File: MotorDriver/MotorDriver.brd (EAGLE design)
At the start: 50 x 50 mm, 52 parts, among them CN1 53375-0610, Q1 BUK7Y7R8-80EX, Q2 BUK7Y7R8-80EX, Q3 BUK7Y7R8-80EX, Q4 BUK7Y7R8-80EX, Q5 BUK7Y7R8-80EX, Q6 BUK7Y7R8-80EX, U1 LPC1549JBD48, U2 DRV8320SRTVT, U3 MCP1700T-33, U4 ADR5041

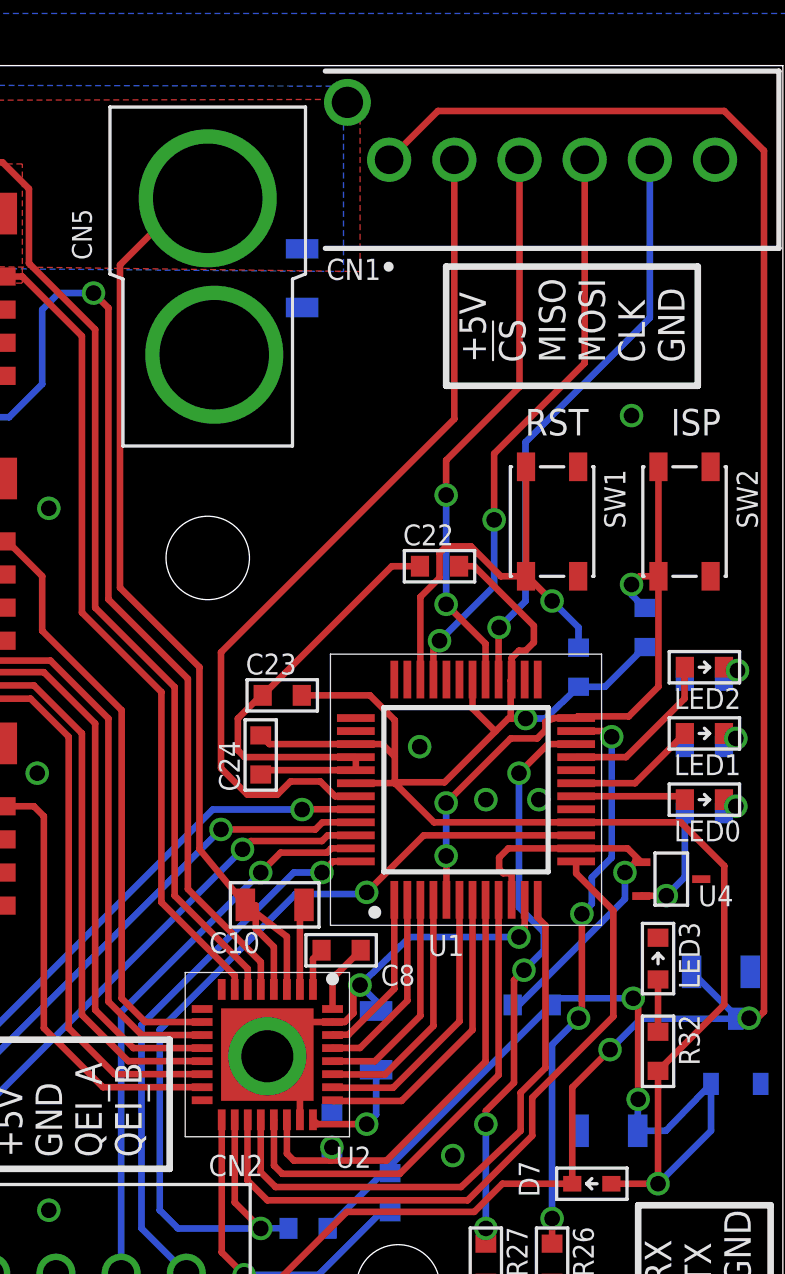
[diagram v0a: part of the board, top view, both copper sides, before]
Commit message: SCT1_OUT[5, 6]を使うために配線を入れ替えた
1:    PWM_CL->MOSI
2:    PWM_CH->RX
22: RX->PWM_CH
33  MOSI->PWM_CL
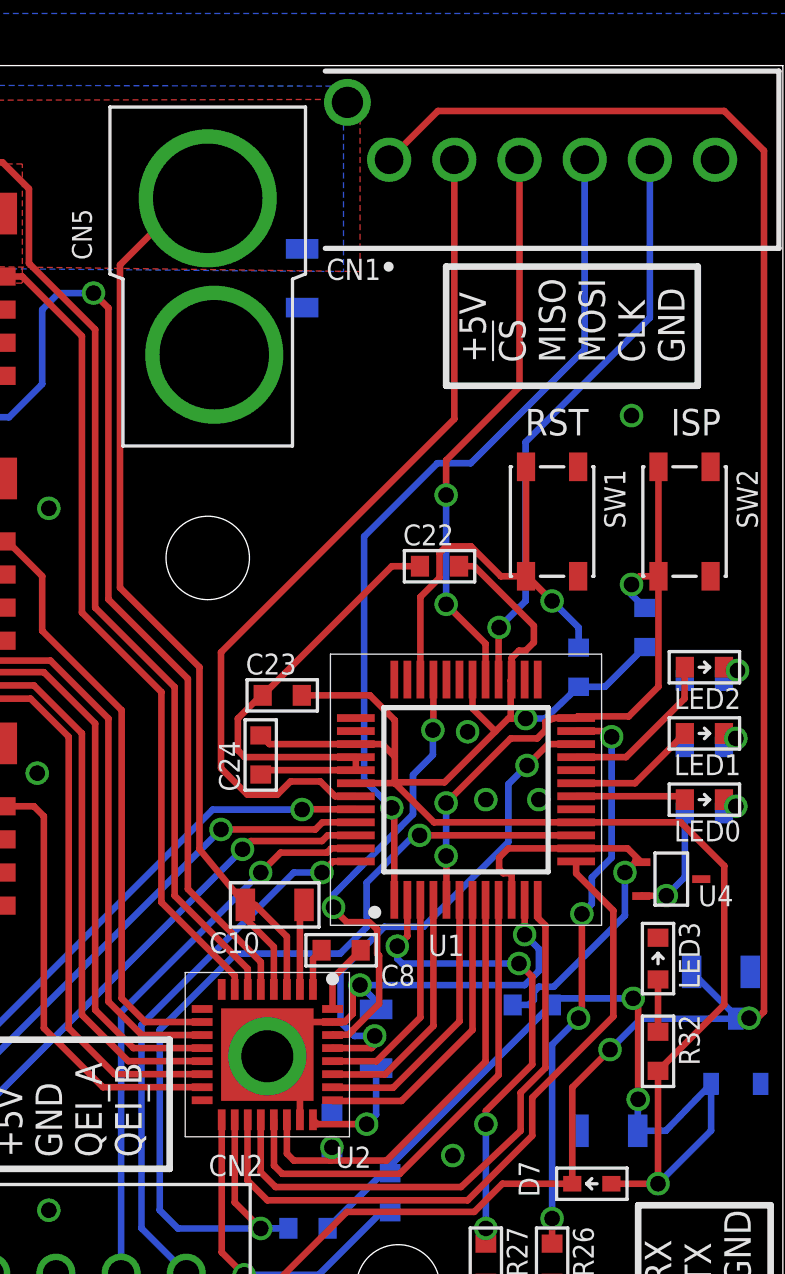
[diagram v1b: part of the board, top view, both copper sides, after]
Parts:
- moved C9 0.06 mm to (34.4, 12.7)
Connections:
- net MOSI: now also U1.1; no longer U1.33
- net PWM_CH: now also U1.22; no longer U1.2
- net PWM_CL: now also U1.33; no longer U1.1
- net RX: now also U1.2; no longer U1.22
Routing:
- net PWM_CH: track 7.49 -> 19.5 mm, vias 0 -> 2
- net PWM_CL: track 6.52 -> 17.5 mm, vias 0 -> 2
- net MOSI: track 22.3 -> 33.1 mm, vias 2 -> 1
- net RX: track 22.0 -> 18.8 mm
- net GND: track 42.2 -> 43.9 mm
- net SDO: track 35.8 -> 36.8 mm
- net VREF: track 15.6 -> 16.2 mm

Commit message: FETのゲートソース間に抵抗を追加
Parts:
- added R10, R11, R12, R7, R8, R9: 10k, Passive:1608
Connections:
- net GH_A: now also R11.2
- net GH_B: now also R9.2
- net GH_C: now also R7.2
- net GL_A: now also R12.2
- net GL_B: now also R10.2
- net GL_C: now also R8.2
- net GND: now also R10.1, R12.1, R8.1
- net SH_A: now also R11.1
- net SH_B: now also R9.1
- net SH_C: now also R7.1
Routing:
- net GND: track 43.9 -> 45.6 mm, vias 14 -> 15
- net GL_B: track 23.1 -> 24.8 mm, vias 0 -> 1
- net GL_C: track 17.0 -> 18.6 mm, vias 0 -> 1
- net GL_A: track 31.6 -> 33.2 mm, vias 0 -> 1
- net SH_C: track 26.3 -> 27.7 mm
- net GH_C: track 31.3 -> 32.7 mm, vias 0 -> 1
- net GH_B: track 33.2 -> 34.1 mm, vias 0 -> 1
- net GH_A: track 52.2 -> 53.2 mm
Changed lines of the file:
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@@
 <attribute name="VALUE" x="24.13" y="35.56" size="0.762" layer="27" font="vector" ratio="17" rot="R90"/>
 </element>
+<element name="R7" library="Passive" package="1608" value="10k" x="13.46875" y="25" rot="MR90"/>
+<element name="R8" library="Passive" package="1608" value="10k" x="18.4375" y="20.625" rot="MR90"/>
+<element name="R9" library="Passive" package="1608" value="10k" x="11.25" y="26.53125" rot="MR180"/>
+<element name="R10" library="Passive" package="1608" value="10k" x="18.4375" y="30.625" rot="MR90"/>
+<element name="R11" library="Passive" package="1608" value="10k" x="11.5625" y="36.5625" rot="MR270"/>
+<element name="R12" library="Passive" package="1608" value="10k" x="18.4375" y="40.9375" rot="MR90"/>
 </elements>
 <signals>
@@
 <via x="15.24" y="40.005" extent="1-16" drill="0.6" shape="octagon"/>
 <via x="15.24" y="41.275" extent="1-16" drill="0.6" shape="octagon"/>
+<contactref element="R11" pad="1"/>
 </signal>
 <signal name="V+">
@@
 <via x="15.24" y="29.845" extent="1-16" drill="0.6" shape="octagon"/>
 <via x="15.24" y="28.575" extent="1-16" drill="0.6" shape="octagon"/>
+<contactref element="R9" pad="1"/>
 </signal>
 <signal name="SH_C">
@@
 <via x="10.795" y="24.13" extent="1-16" drill="0.6" shape="octagon"/>
 <via x="12.065" y="24.13" extent="1-16" drill="0.6" shape="octagon"/>
+<contactref element="R7" pad="1"/>
+<wire x1="13.46875" y1="24.25" x2="13.34875" y2="24.13" width="0.254" layer="16"/>
+<wire x1="13.34875" y1="24.13" x2="12.065" y2="24.13" width="0.254" layer="16"/>
 </signal>
 <signal name="GND">
@@
 <wire x1="33.19" y1="13.315" x2="33.5" y2="13.625" width="0.254" layer="1"/>
 <wire x1="33.19" y1="13.315" x2="32.726" y2="13.315" width="0.254" layer="1"/>
+<contactref element="R8" pad="1"/>
+<contactref element="R10" pad="1"/>
+<contactref element="R12" pad="1"/>
+<wire x1="18.4375" y1="40.1875" x2="18.90625" y2="40.65625" width="0.254" layer="16"/>
+<wire x1="18.90625" y1="40.65625" x2="19.1875" y2="40.65625" width="0.254" layer="16"/>
+<via x="19.1875" y="40.65625" extent="1-16" drill="0.6" shape="octagon"/>
+<wire x1="19.1875" y1="40.65625" x2="19.20375" y2="40.64" width="0.254" layer="1"/>
+<wire x1="19.20375" y1="40.64" x2="19.997" y2="40.64" width="0.254" layer="1"/>
 </signal>
 <signal name="GH_A">
@@
 <wire x1="21.59" y1="37.7825" x2="20.32" y2="36.5125" width="0.254" layer="16"/>
 <wire x1="20.32" y1="36.5125" x2="10.9855" y2="36.5125" width="0.254" layer="16"/>
-<wire x1="10.9855" y1="36.5125" x2="10.033" y2="37.465" width="0.254" layer="16"/>
+<wire x1="10.9855" y1="36.5125" x2="10.920875" y2="36.577125" width="0.254" layer="16"/>
+<wire x1="10.920875" y1="36.577125" x2="10.033" y2="37.465" width="0.254" layer="16"/>
 <wire x1="10.033" y1="37.465" x2="10.033" y2="41.529" width="0.254" layer="16"/>
 <wire x1="10.033" y1="41.529" x2="10.3505" y2="41.8465" width="0.254" layer="16"/>
@@
 <wire x1="10.3505" y1="41.8465" x2="11.0435" y2="41.8465" width="0.254" layer="1"/>
 <wire x1="11.0435" y1="41.8465" x2="11.107" y2="41.91" width="0.254" layer="1"/>
+<contactref element="R11" pad="2"/>
+<wire x1="11.5625" y1="35.8125" x2="11.5625" y2="35.9355" width="0.254" layer="16"/>
+<wire x1="11.5625" y1="35.9355" x2="10.9855" y2="36.5125" width="0.254" layer="16"/>
 </signal>
 <signal name="GL_A">
@@
 <wire x1="19.997" y1="41.91" x2="20.828" y2="41.91" width="0.254" layer="1"/>
 <wire x1="20.828" y1="41.91" x2="23.114" y2="39.624" width="0.254" layer="1"/>
+<contactref element="R12" pad="2"/>
+<wire x1="18.4375" y1="41.6875" x2="18.65625" y2="41.90625" width="0.254" layer="16"/>
+<wire x1="18.65625" y1="41.90625" x2="19.4375" y2="41.90625" width="0.254" layer="16"/>
+<via x="19.4375" y="41.90625" extent="1-16" drill="0.6" shape="octagon"/>
+<wire x1="19.4375" y1="41.90625" x2="19.44125" y2="41.91" width="0.254" layer="1"/>
+<wire x1="19.44125" y1="41.91" x2="19.997" y2="41.91" width="0.254" layer="1"/>
 </signal>
 <signal name="GH_B">
@@
 <wire x1="21.6535" y1="26.7335" x2="13.0175" y2="26.7335" width="0.254" layer="1"/>
 <wire x1="13.0175" y1="26.7335" x2="12.446" y2="27.305" width="0.254" layer="1"/>
-<wire x1="12.446" y1="27.305" x2="12.446" y2="30.861" width="0.254" layer="1"/>
+<wire x1="12.446" y1="27.305" x2="12.446" y2="27.53125" width="0.254" layer="1"/>
+<wire x1="12.446" y1="27.53125" x2="12.446" y2="30.861" width="0.254" layer="1"/>
 <wire x1="12.446" y1="30.861" x2="11.557" y2="31.75" width="0.254" layer="1"/>
 <wire x1="11.557" y1="31.75" x2="11.107" y2="31.75" width="0.254" layer="1"/>
+<contactref element="R9" pad="2"/>
+<wire x1="12" y1="26.53125" x2="12.25" y2="26.78125" width="0.254" layer="16"/>
+<via x="12.25" y="26.78125" extent="1-16" drill="0.6" shape="octagon"/>
+<wire x1="12.25" y1="26.78125" x2="12.446" y2="26.97725" width="0.254" layer="1"/>
+<wire x1="12.446" y1="26.97725" x2="12.446" y2="27.305" width="0.254" layer="1"/>
 </signal>
 <signal name="GL_B">
@@
 <wire x1="21.59" y1="30.4165" x2="20.2565" y2="31.75" width="0.254" layer="1"/>
 <wire x1="20.2565" y1="31.75" x2="19.997" y2="31.75" width="0.254" layer="1"/>
+<contactref element="R10" pad="2"/>
+<wire x1="18.4375" y1="31.375" x2="18.8125" y2="31.75" width="0.254" layer="16"/>
+<wire x1="18.8125" y1="31.75" x2="19.46875" y2="31.75" width="0.254" layer="16"/>
+<via x="19.46875" y="31.75" extent="1-16" drill="0.6" shape="octagon"/>
+<wire x1="19.46875" y1="31.75" x2="19.997" y2="31.75" width="0.254" layer="1"/>
 </signal>
 <signal name="GH_C">
@@
 <wire x1="11.107" y1="21.59" x2="13.97" y2="24.453" width="0.254" layer="1"/>
 <wire x1="13.97" y1="24.453" x2="13.97" y2="25.273" width="0.254" layer="1"/>
-<wire x1="13.97" y1="25.273" x2="14.9225" y2="26.2255" width="0.254" layer="1"/>
+<wire x1="13.97" y1="25.273" x2="14.7235" y2="26.0265" width="0.254" layer="1"/>
+<wire x1="14.7235" y1="26.0265" x2="14.9225" y2="26.2255" width="0.254" layer="1"/>
 <wire x1="14.9225" y1="26.2255" x2="21.2725" y2="26.2255" width="0.254" layer="1"/>
 <wire x1="21.2725" y1="26.2255" x2="23.114" y2="24.384" width="0.254" layer="1"/>
+<contactref element="R7" pad="2"/>
+<wire x1="13.46875" y1="25.75" x2="13.6875" y2="25.96875" width="0.254" layer="16"/>
+<wire x1="13.6875" y1="25.96875" x2="13.8125" y2="25.96875" width="0.254" layer="16"/>
+<via x="13.8125" y="25.96875" extent="1-16" drill="0.6" shape="octagon"/>
+<wire x1="13.8125" y1="25.96875" x2="13.87025" y2="26.0265" width="0.254" layer="1"/>
+<wire x1="13.87025" y1="26.0265" x2="14.7235" y2="26.0265" width="0.254" layer="1"/>
 </signal>
 <signal name="GL_C">
@@
 <wire x1="21.6535" y1="21.209" x2="21.2725" y2="21.59" width="0.254" layer="1"/>
 <wire x1="21.2725" y1="21.59" x2="19.997" y2="21.59" width="0.254" layer="1"/>
+<contactref element="R8" pad="2"/>
+<wire x1="18.4375" y1="21.375" x2="18.65625" y2="21.59375" width="0.254" layer="16"/>
+<wire x1="18.65625" y1="21.59375" x2="19.125" y2="21.59375" width="0.254" layer="16"/>
+<via x="19.125" y="21.59375" extent="1-16" drill="0.6" shape="octagon"/>
+<wire x1="19.125" y1="21.59375" x2="19.12875" y2="21.59" width="0.254" layer="1"/>
+<wire x1="19.12875" y1="21.59" x2="19.997" y2="21.59" width="0.254" layer="1"/>
 </signal>
 <signal name="+3V3">

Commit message: nya-n
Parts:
- C1, C10, C19, C2, C20, C3, C6, C9: device MotorDriver_Rev1:PASSIVE_2012 -> MotorDriver:C2012
- C22, C23, C24: device Passive:1608 -> MotorDriver:C1608
- C8: device MotorDriver_Rev1:PASSIVE_1608 -> MotorDriver:C1608
- CN1: device MotorDriver:53375-0610_53375-0610 -> MotorDriver:53375-0610
- D7: device MotorDriver_Rev1:DIODE_SOD523$1 -> MotorDriver:DIODE_SOD523
- LED0, LED1, LED2: device Opto:1608 -> MotorDriver:LED1608
- LED3: device Opto:1611 -> MotorDriver:LED1608
- R1, R10, R11, R12, R17, R2, R21, R23, R26, R27, R3, R32, R4, R5, R6, R7, R8, R9: device Passive:1608 -> MotorDriver:R1608
- U1: device LPC1549JBD48:QFP50P900X900X160-48N -> MotorDriver:QFP48
- U2: device DRV8320SRTVT:QFN50P500X500X80-33N -> MotorDriver:DRV8320SRTVT
